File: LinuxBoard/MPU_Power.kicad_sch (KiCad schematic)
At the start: 46 parts, among them U1 STM32MP151AAB3

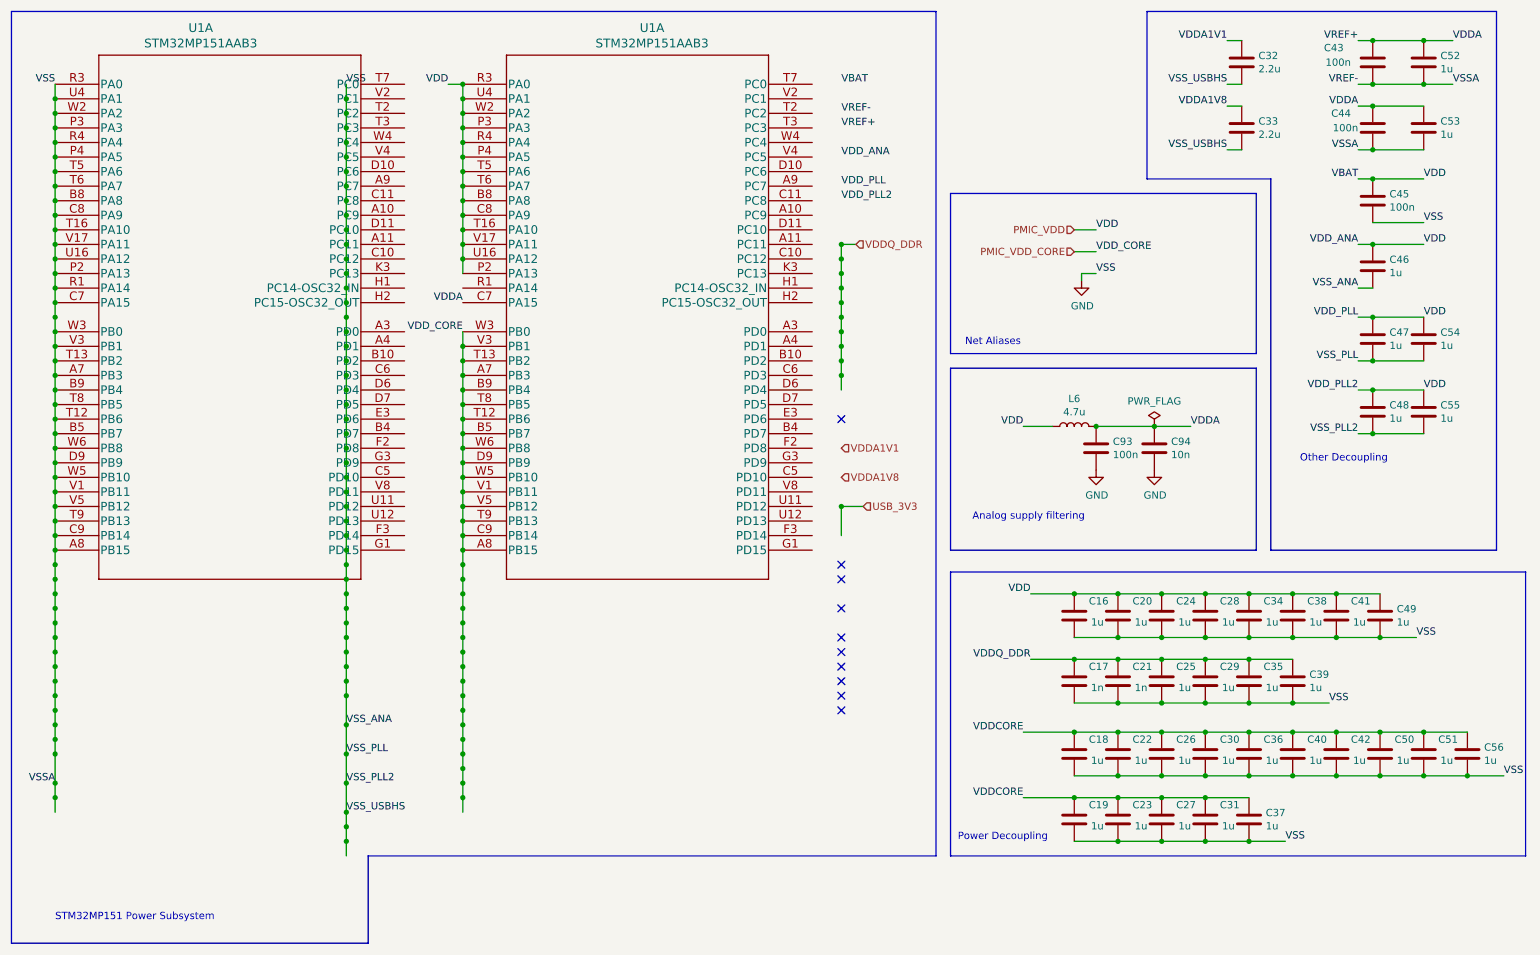
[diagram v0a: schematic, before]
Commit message: Fix ERC errors and reorganize directory
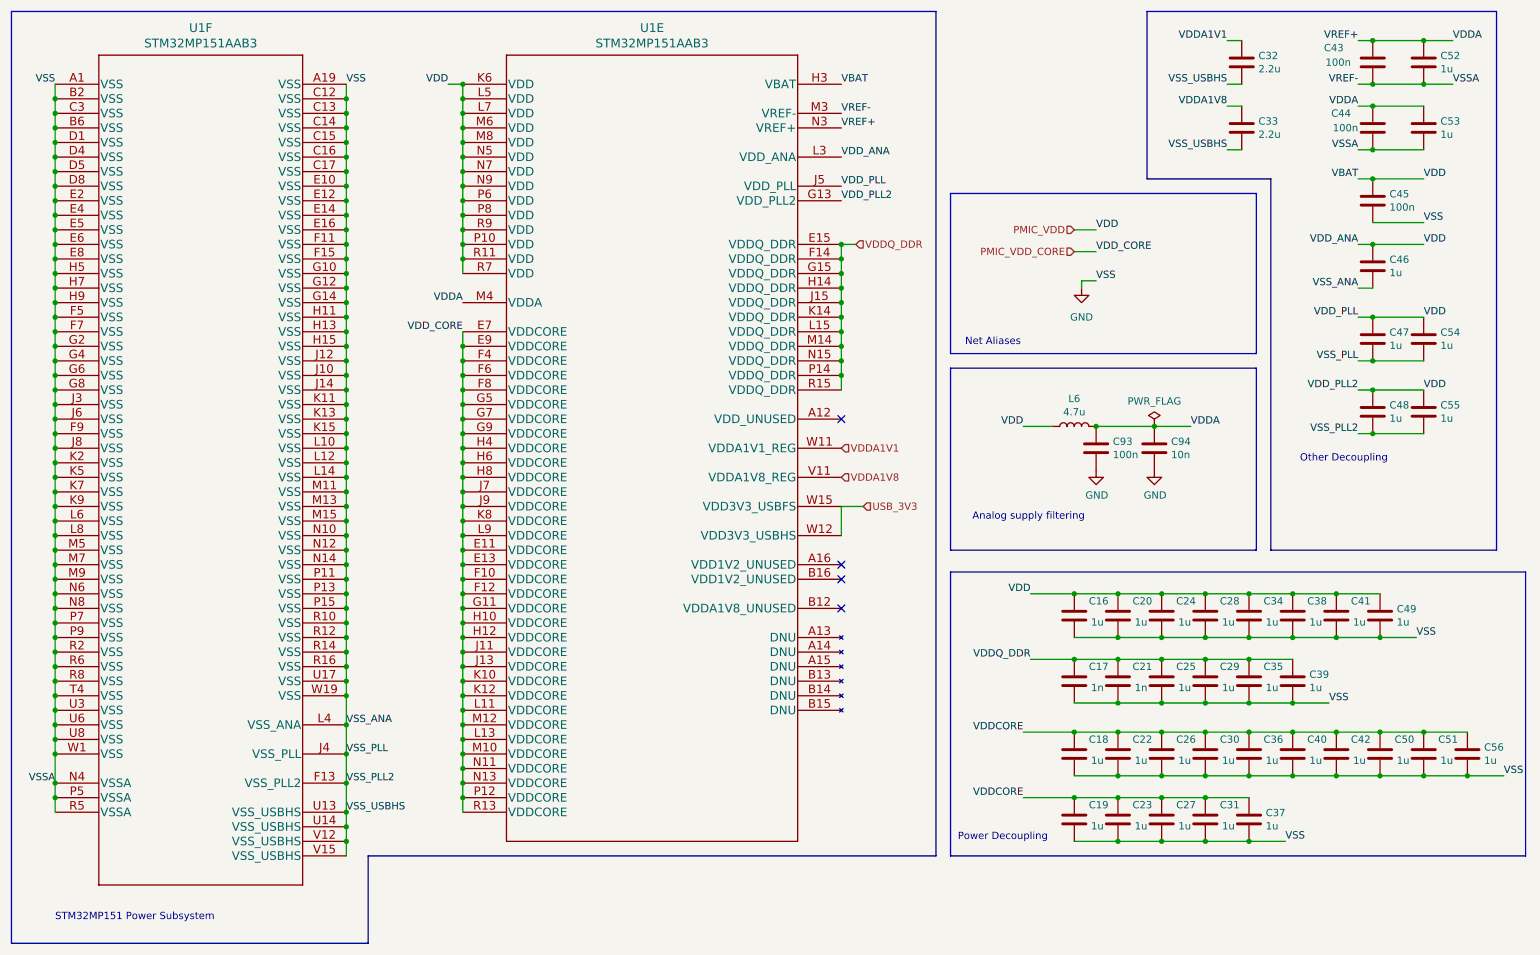
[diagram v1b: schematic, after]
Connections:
- net GND: now also U1.A1 (VSS), U1.A19 (VSS), U1.B2 (VSS), U1.B6 (VSS), U1.C12 (VSS), U1.C13 (VSS), U1.C14 (VSS), U1.C15 (VSS), U1.C16 (VSS), U1.C17 (VSS), U1.C3 (VSS), U1.D1 (VSS), U1.D4 (VSS), U1.D5 (VSS), U1.D8 (VSS), U1.E10 (VSS), U1.E12 (VSS), U1.E14 (VSS), U1.E16 (VSS), U1.E2 (VSS), U1.E4 (VSS), U1.E5 (VSS), U1.E6 (VSS), U1.E8 (VSS), U1.F11 (VSS), U1.F13 (VSS_PLL2), U1.F15 (VSS), U1.F5 (VSS), U1.F7 (VSS), U1.F9 (VSS), U1.G10 (VSS), U1.G12 (VSS), U1.G14 (VSS), U1.G2 (VSS), U1.G4 (VSS), U1.G6 (VSS), U1.G8 (VSS), U1.H11 (VSS), U1.H13 (VSS), U1.H15 (VSS), U1.H5 (VSS), U1.H7 (VSS), U1.H9 (VSS), U1.J10 (VSS), U1.J12 (VSS), U1.J14 (VSS), U1.J3 (VSS), U1.J4 (VSS_PLL), U1.J6 (VSS), U1.J8 (VSS), U1.K11 (VSS), U1.K13 (VSS), U1.K15 (VSS), U1.K2 (VSS), U1.K5 (VSS), U1.K7 (VSS), U1.K9 (VSS), U1.L10 (VSS), U1.L12 (VSS), U1.L14 (VSS), U1.L4 (VSS_ANA), U1.L6 (VSS), U1.L8 (VSS), U1.M11 (VSS), U1.M13 (VSS), U1.M15 (VSS), U1.M3 (VREF-), U1.M5 (VSS), U1.M7 (VSS), U1.M9 (VSS), U1.N10 (VSS), U1.N12 (VSS), U1.N14 (VSS), U1.N4 (VSSA), U1.N6 (VSS), U1.N8 (VSS), U1.P11 (VSS), U1.P13 (VSS), U1.P15 (VSS), U1.P5 (VSSA), U1.P7 (VSS), U1.P9 (VSS), U1.R10 (VSS), U1.R12 (VSS), U1.R14 (VSS), U1.R16 (VSS), U1.R2 (VSS), U1.R5 (VSSA), U1.R6 (VSS), U1.R8 (VSS), U1.T4 (VSS), U1.U13 (VSS_USBHS), U1.U14 (VSS_USBHS), U1.U17 (VSS), U1.U3 (VSS), U1.U6 (VSS), U1.U8 (VSS), U1.V12 (VSS_USBHS), U1.V15 (VSS_USBHS), U1.W1 (VSS), U1.W19 (VSS); no longer U1.A7 (PB3), U1.A8 (PB15), U1.B5 (PB7), U1.B8 (PA8), U1.B9 (PB4), U1.C7 (PA15), U1.C8 (PA9), U1.C9 (PB14), U1.D9 (PB9), U1.P2 (PA13), U1.P3 (PA3), U1.P4 (PA5), U1.R1 (PA14), U1.R3 (PA0), U1.R4 (PA4), U1.T12 (PB6), U1.T13 (PB2), U1.T16 (PA10), U1.T5 (PA6), U1.T6 (PA7), U1.T8 (PB5), U1.T9 (PB13), U1.U16 (PA12), U1.U4 (PA1), U1.V1 (PB11), U1.V17 (PA11), U1.V3 (PB1), U1.V5 (PB12), U1.W2 (PA2), U1.W3 (PB0), U1.W5 (PB10), U1.W6 (PB8)
- net PMIC_VDD: now also U1.G13 (VDD_PLL2), U1.H3 (VBAT), U1.J5 (VDD_PLL), U1.K6 (VDD), U1.L3 (VDD_ANA), U1.L5 (VDD), U1.L7 (VDD), U1.M6 (VDD), U1.M8 (VDD), U1.N5 (VDD), U1.N7 (VDD), U1.N9 (VDD), U1.P10 (VDD), U1.P6 (VDD), U1.P8 (VDD), U1.R11 (VDD), U1.R7 (VDD), U1.R9 (VDD); no longer U1.B8 (PA8), U1.C8 (PA9), U1.P2 (PA13), U1.P3 (PA3), U1.P4 (PA5), U1.R3 (PA0), U1.R4 (PA4), U1.T16 (PA10), U1.T5 (PA6), U1.T6 (PA7), U1.U16 (PA12), U1.U4 (PA1), U1.V17 (PA11), U1.W2 (PA2)
- net PMIC_VDD_CORE: now also U1.E11 (VDDCORE), U1.E13 (VDDCORE), U1.E7 (VDDCORE), U1.E9 (VDDCORE), U1.F10 (VDDCORE), U1.F12 (VDDCORE), U1.F4 (VDDCORE), U1.F6 (VDDCORE), U1.F8 (VDDCORE), U1.G11 (VDDCORE), U1.G5 (VDDCORE), U1.G7 (VDDCORE), U1.G9 (VDDCORE), U1.H10 (VDDCORE), U1.H12 (VDDCORE), U1.H4 (VDDCORE), U1.H6 (VDDCORE), U1.H8 (VDDCORE), U1.J11 (VDDCORE), U1.J13 (VDDCORE), U1.J7 (VDDCORE), U1.J9 (VDDCORE), U1.K10 (VDDCORE), U1.K12 (VDDCORE), U1.K8 (VDDCORE), U1.L11 (VDDCORE), U1.L13 (VDDCORE), U1.L9 (VDDCORE), U1.M10 (VDDCORE), U1.M12 (VDDCORE), U1.N11 (VDDCORE), U1.N13 (VDDCORE), U1.P12 (VDDCORE), U1.R13 (VDDCORE); no longer U1.A7 (PB3), U1.A8 (PB15), U1.B5 (PB7), U1.B9 (PB4), U1.C9 (PB14), U1.D9 (PB9), U1.T12 (PB6), U1.T13 (PB2), U1.T8 (PB5), U1.T9 (PB13), U1.V1 (PB11), U1.V3 (PB1), U1.V5 (PB12), U1.W3 (PB0), U1.W5 (PB10), U1.W6 (PB8)
- net USB_3V3: now also U1.W12 (VDD3V3_USBHS), U1.W15 (VDD3V3_USBFS)
- net VDDA: now also U1.M4 (VDDA), U1.N3 (VREF+); no longer U1.C7 (PA15)
- net VDDA1V1: now also U1.W11 (VDDA1V1_REG)
- net VDDA1V8: now also U1.V11 (VDDA1V8_REG)
- net VDDQ_DDR: now also U1.E15 (VDDQ_DDR), U1.F14 (VDDQ_DDR), U1.G15 (VDDQ_DDR), U1.H14 (VDDQ_DDR), U1.J15 (VDDQ_DDR), U1.K14 (VDDQ_DDR), U1.L15 (VDDQ_DDR), U1.M14 (VDDQ_DDR), U1.N15 (VDDQ_DDR), U1.P14 (VDDQ_DDR), U1.R15 (VDDQ_DDR)
- no-connect marks 10 -> 4
